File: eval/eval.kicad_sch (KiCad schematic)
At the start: 5 parts, among them J1 TC2030, U9 STM32G0B1CBTx

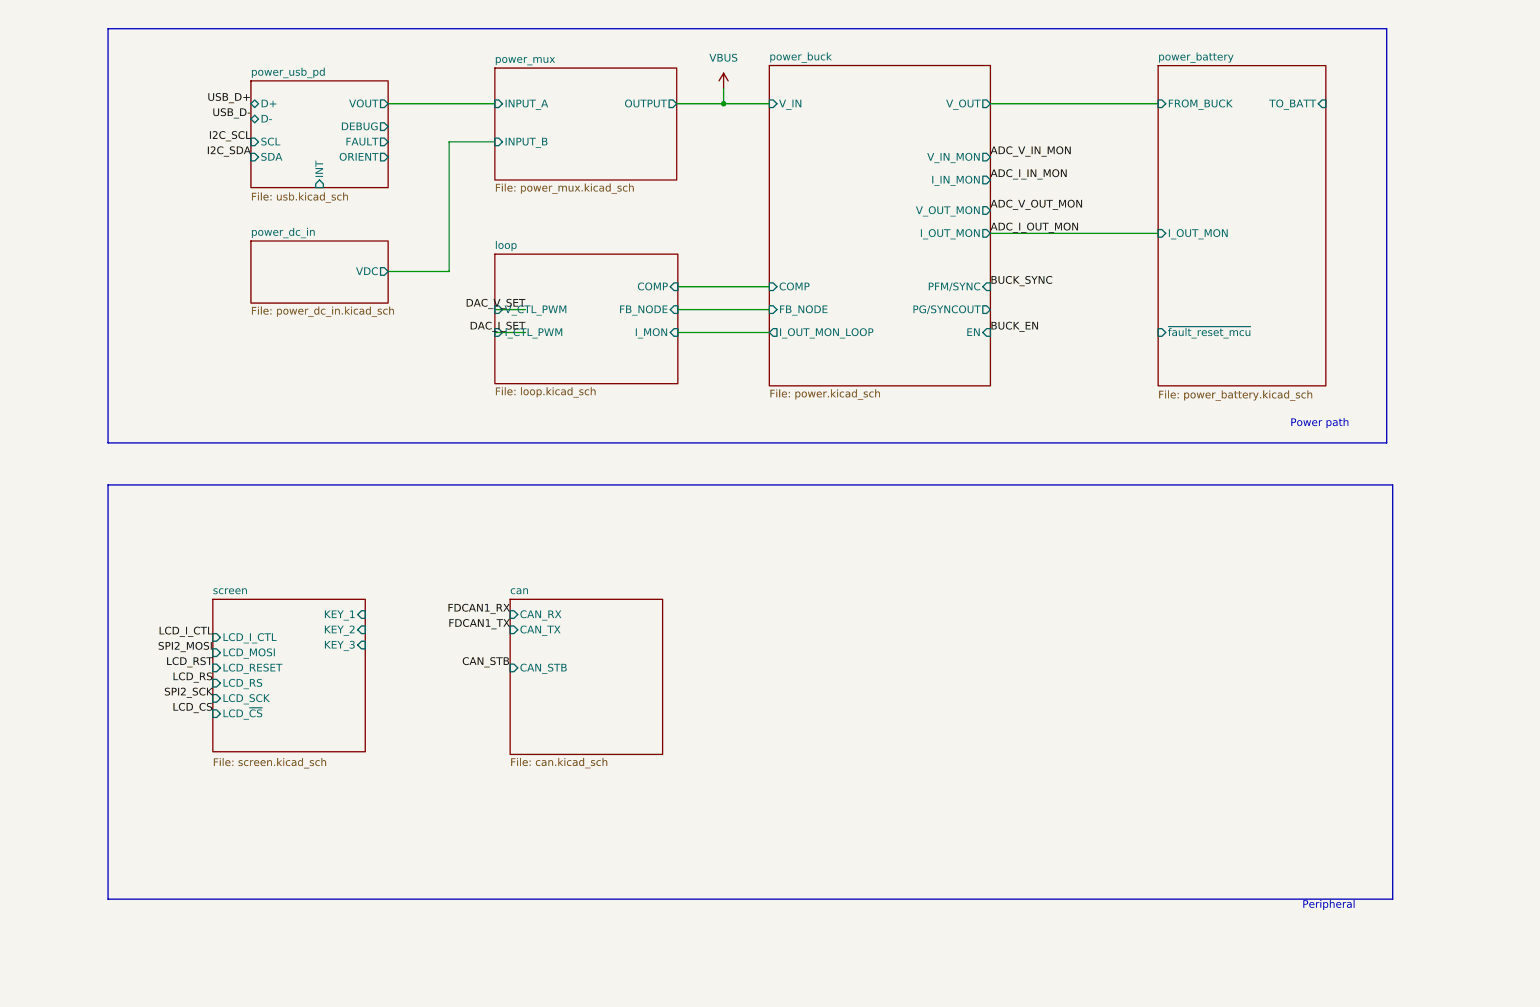
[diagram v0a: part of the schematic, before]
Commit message: [layout] group every function group together, ready for layout
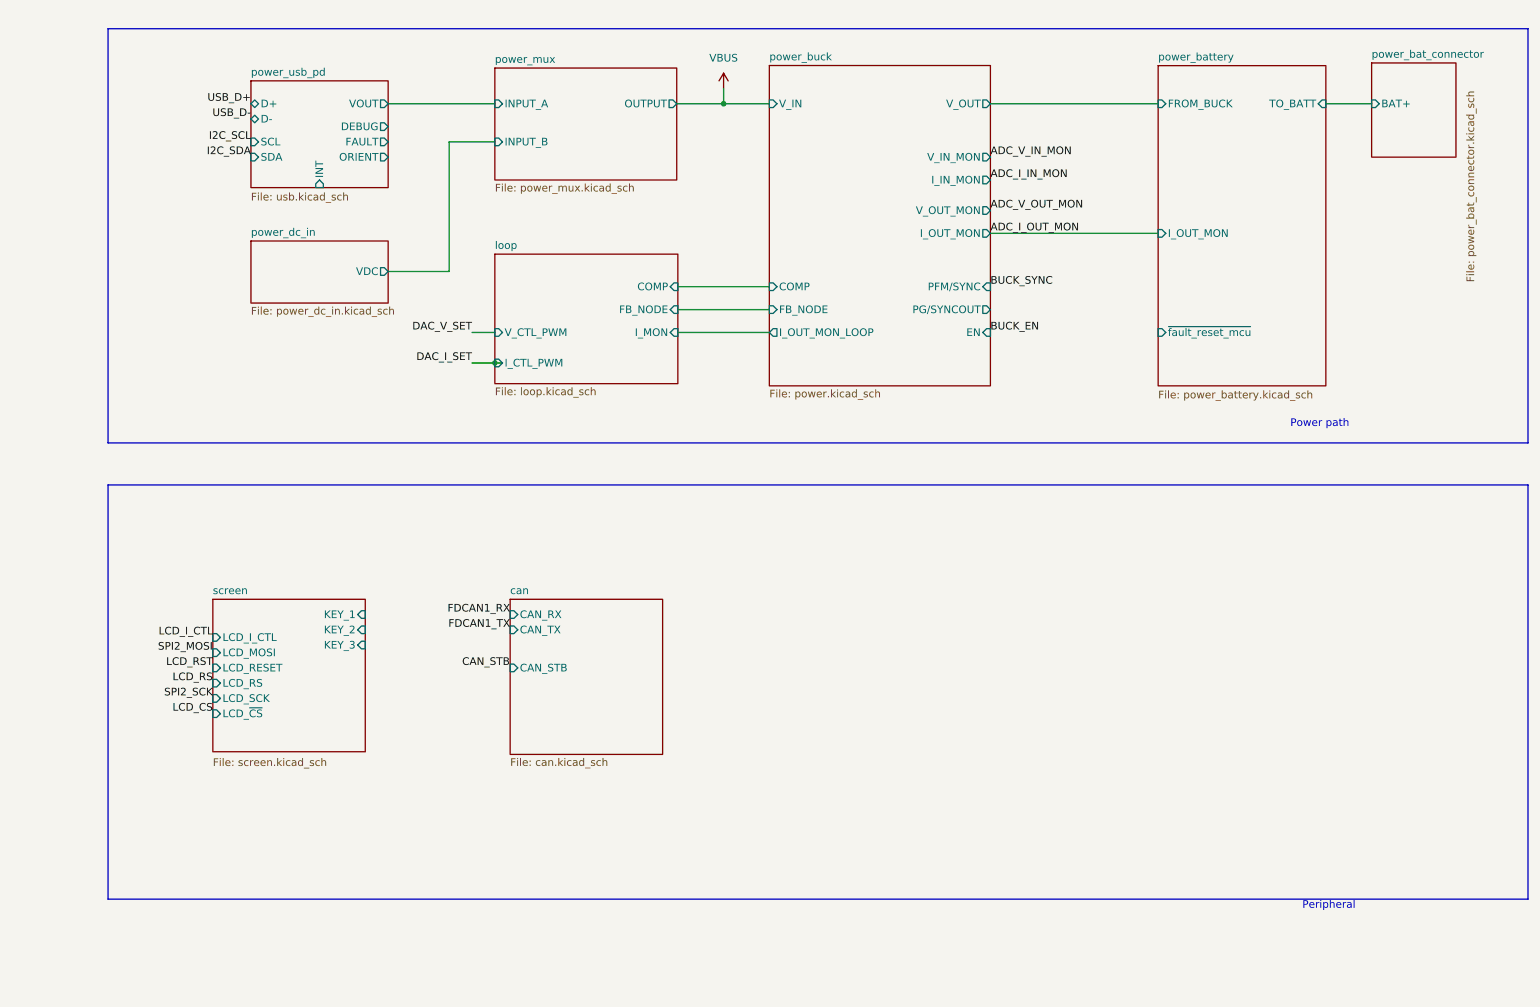
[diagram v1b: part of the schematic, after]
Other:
- added sheet power_bat_connector (power_bat_connector.kicad_sch)
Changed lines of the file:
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@@
 	(rectangle
 		(start 151.46 38.3)
-		(end 364.46 107.3)
+		(end 388 107.3)
 		(stroke
 			(width 0)
@@
 	(rectangle
 		(start 151.46 114.3)
-		(end 365.46 183.3)
+		(end 388 183.3)
 		(stroke
 			(width 0)
@@
 	)
 	(junction
+		(at 215.9 93.98)
+		(diameter 0)
+		(color 0 0 0 0)
+	)
+	(junction
 		(at 88.9 43.18)
 		(diameter 0)
@@
 	(wire
 		(pts
+			(xy 212.09 93.98) (xy 215.9 93.98)
+		)
+		(stroke
+			(width 0)
+			(type default)
+		)
+	)
+	(wire
+		(pts
 			(xy 198.12 78.74) (xy 208.28 78.74)
 		)
@@
 	(wire
 		(pts
-			(xy 215.9 88.9) (xy 220.98 88.9)
-		)
-		(stroke
-			(width 0)
-			(type default)
-		)
-	)
-	(wire
-		(pts
 			(xy 198.12 50.8) (xy 215.9 50.8)
 		)
@@
 	(wire
 		(pts
+			(xy 354.33 50.8) (xy 361.95 50.8)
+		)
+		(stroke
+			(width 0)
+			(type default)
+		)
+	)
+	(wire
+		(pts
 			(xy 80.01 157.48) (xy 80.01 154.94)
 		)
@@
 	(wire
 		(pts
+			(xy 215.9 93.98) (xy 217.17 93.98)
+		)
+		(stroke
+			(width 0)
+			(type default)
+		)
+	)
+	(wire
+		(pts
 			(xy 254 48.26) (xy 254 50.8)
 		)
@@
 	(wire
 		(pts
-			(xy 215.9 85.09) (xy 220.98 85.09)
+			(xy 215.9 88.9) (xy 212.09 88.9)
 		)
 		(stroke
@@
 	)
 	(label "DAC_I_SET"
-		(at 220.98 88.9 180)
+		(at 212.09 93.98 180)
 		(effects
 			(font
@@
 	)
 	(label "DAC_V_SET"
-		(at 220.98 85.09 180)
+		(at 212.09 88.9 180)
 		(effects
 			(font
@@
 	)
 	(sheet
+		(at 361.95 44)
+		(size 14.05 15.69)
+		(exclude_from_sim no)
+		(in_bom yes)
+		(on_board yes)
+		(dnp no)
+		(stroke
+			(width 0.1524)
+			(type solid)
+		)
+		(fill
+			(color 0 0 0 0)
+		)
+		(property "Sheetname" "power_bat_connector"
+			(at 361.95 43.2884 0)
+			(show_name no)
+			(do_not_autoplace no)
+			(effects
+				(font
+					(size 1.27 1.27)
+				)
+				(justify left bottom)
+			)
+		)
+		(property "Sheetfile" "power_bat_connector.kicad_sch"
+			(at 377.698 80.518 90)
+			(show_name no)
+			(do_not_autoplace no)
+			(effects
+				(font
+					(size 1.27 1.27)
+				)
+				(justify left top)
+			)
+		)
+		(pin "BAT+" input
+			(at 361.95 50.8 180)
+			(effects
+				(font
+					(size 1.27 1.27)
+				)
+				(justify left)
+			)
+		)
+		(instances
+			(project "eval"
+				(path "/8b023652-20db-48ce-ad53-bc2d9a4e5dd4"
+					(page "15")
+				)
+			)
+		)
+	)
+	(sheet
 		(at 215.9 75.85)
 		(size 30.48 21.58)
@@
 		)
 		(pin "I_CTL_PWM" input
-			(at 215.9 88.9 180)
+			(at 215.9 93.98 180)
 			(effects
 				(font
@@
 		)
 		(pin "V_CTL_PWM" input
-			(at 215.9 85.09 180)
-			(effects
-				(font
+			(at 215.9 88.9 180)
+			(effects
+				(font

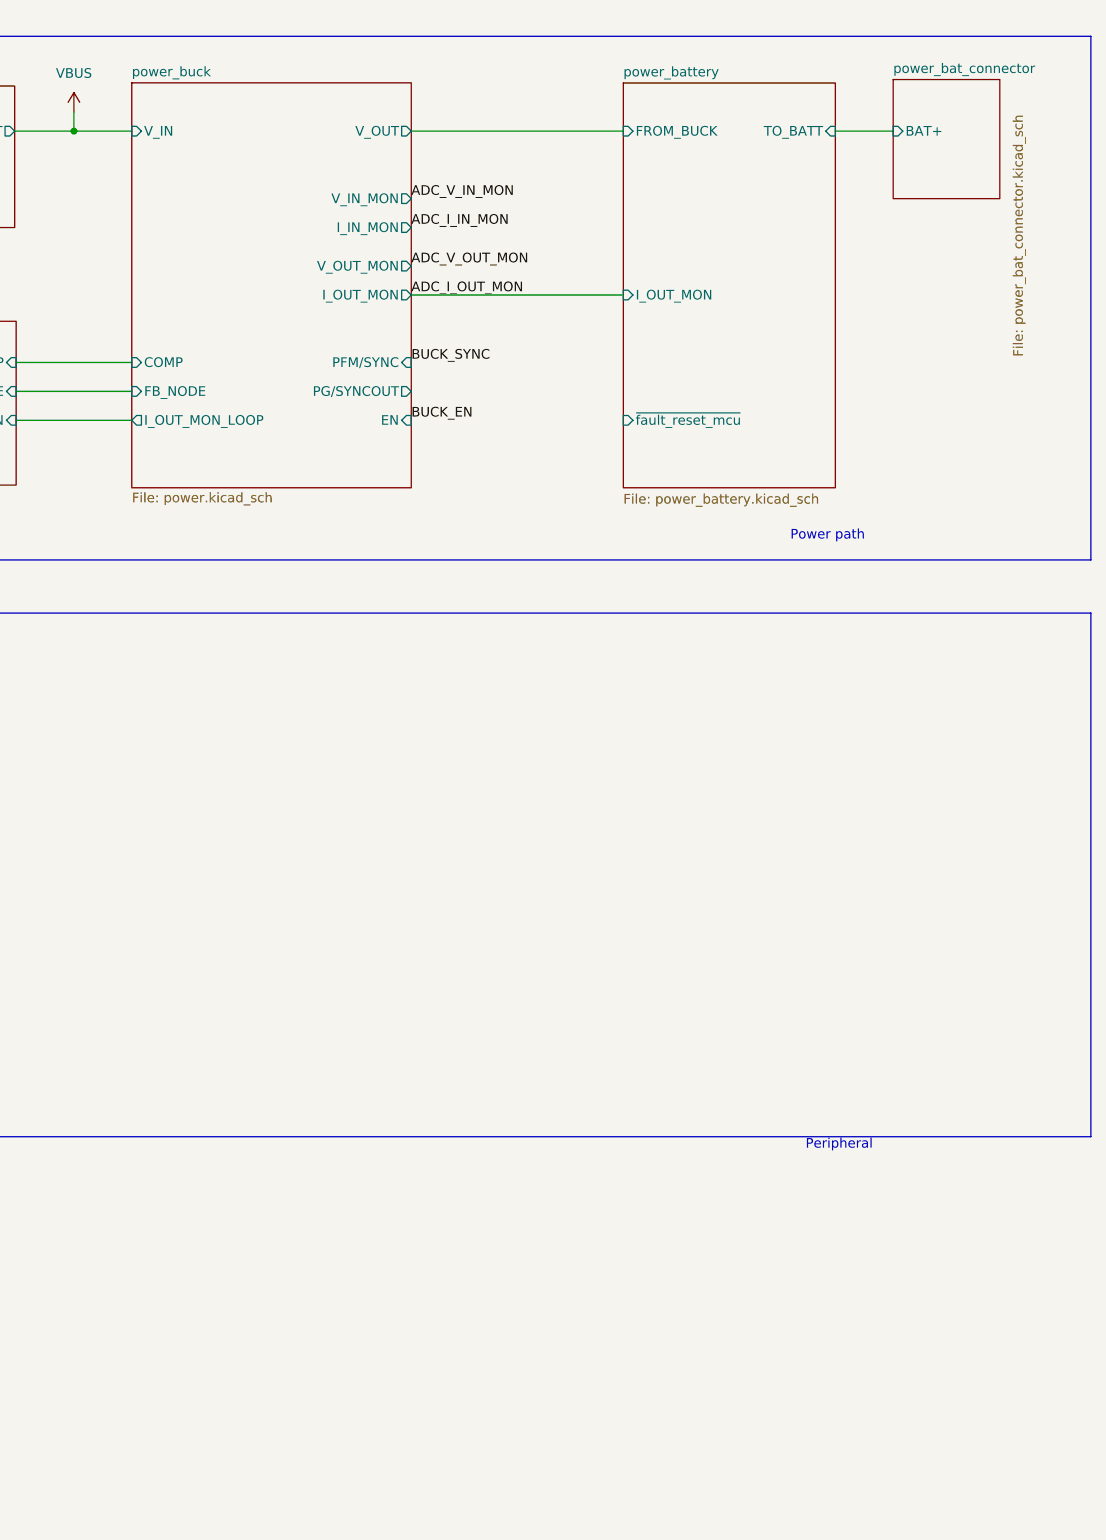
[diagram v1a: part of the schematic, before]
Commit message: [layout] fan on bottom side, power area on top
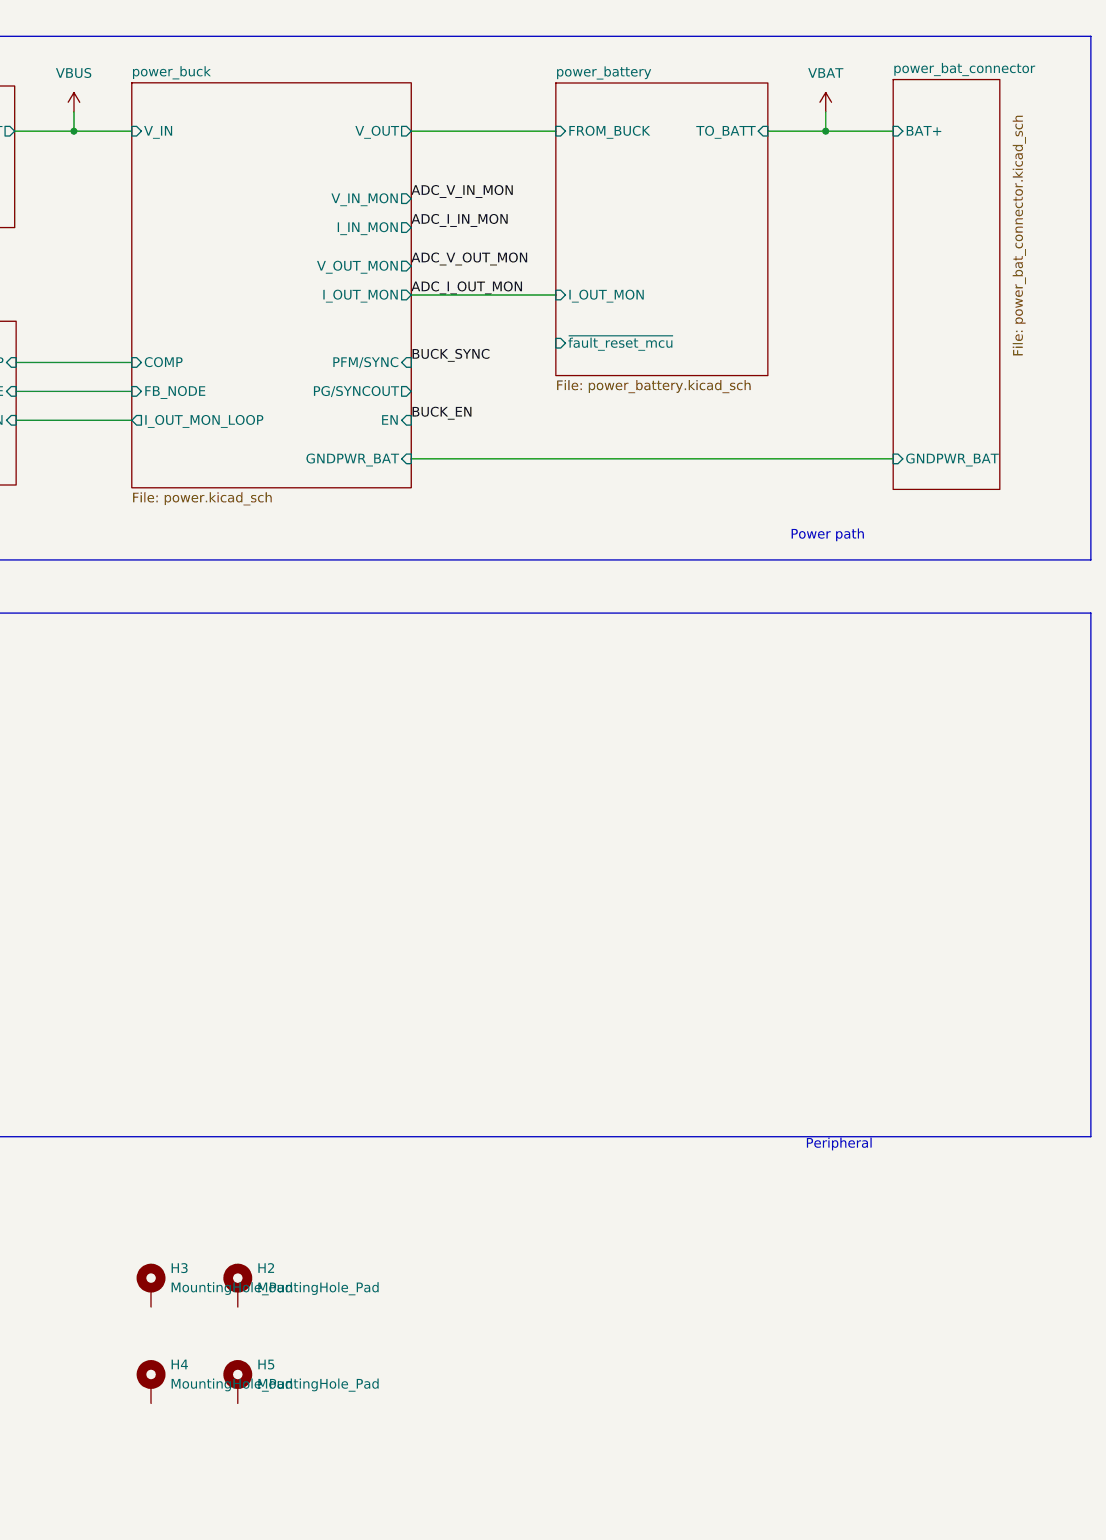
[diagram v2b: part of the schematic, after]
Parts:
- added H2, H3, H4, H5: MountingHole_Pad, MountingHole:MountingHole_2.2mm_M2_Pad_Via, symbol Mechanical:MountingHole_Pad
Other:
- sheet power_bat_connector ports: added GNDPWR_BAT; removed none
- sheet power_buck ports: added GNDPWR_BAT; removed none

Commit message: [layout] layout completed, ready for trace
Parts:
- added BZ1: Buzzer, symbol Device:Buzzer
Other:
- added sheet ntc (ntc.kicad_sch)
- added sheet ntc1 (ntc.kicad_sch)
- added sheet ntc2 (ntc.kicad_sch)

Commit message: [trace] add high power trace
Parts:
- renumbered C19 to C1, C20 to C2, C21 to C3, H3 to H1, H4 to H2, H2 to H3, H5 to H4, U9 to U1
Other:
- sheet loop ports: added I_CTL, V_CTL; removed I_CTL_PWM, V_CTL_PWM

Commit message: [trace] Add USB trace (with impedance control)
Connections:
- net ADC_I_IN_MON: now also U1.12 (PA1); no longer U1.13 (PA2)
- net ADC_I_OUT_MON: now also U1.19 (PB0); no longer U1.11 (PA0)
- net ADC_V_IN_MON: now also U1.11 (PA0); no longer U1.14 (PA3)
- net ADC_V_OUT_MON: no longer U1.12 (PA1)
- net ADC_V_OUT+_MON: now reaches U1.20 (PB1)
- net ADC_V_OUT-_MON: now reaches U1.21 (PB2)
- new net ADC_NTC_0: U1.13 (PA2)
- new net ADC_NTC_1: U1.14 (PA3)
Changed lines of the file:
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@@
-	(wire
-		(pts
-			(xy 107.95 83.82) (xy 107.95 82.55)
-		)
-		(stroke
-			(width 0)
-			(type default)
-		)
-	)
 	(wire
 		(pts
@@
 	)
 	(label "ADC_I_IN_MON"
+		(at 107.95 62.23 0)
+		(effects
+			(font
+				(size 1.27 1.27)
+			)
+			(justify left bottom)
+		)
+	)
+	(label "ADC_NTC_2"
+		(at 133.35 77.47 0)
+		(effects
+			(font
+				(size 1.27 1.27)
+			)
+			(justify left bottom)
+		)
+	)
+	(label "ADC_I_IN_MON"
 		(at 298.45 63.5 0)
 		(effects
@@
 		)
 	)
-	(label "ADC_I_OUT_MON"
+	(label "ADC_V_IN_MON"
 		(at 107.95 59.69 0)
 		(effects
@@
 		)
 	)
-	(label "ADC_I_IN_MON"
-		(at 107.95 64.77 0)
-		(effects
-			(font
-				(size 1.27 1.27)
-			)
-			(justify left bottom)
-		)
-	)
 	(label "ADC_V_OUT_MON"
 		(at 298.45 68.58 0)
@@
 		)
 	)
+	(label "ADC_I_OUT_MON"
+		(at 107.95 102.87 0)
+		(effects
+			(font
+				(size 1.27 1.27)
+			)
+			(justify left bottom)
+		)
+	)
 	(label "SYS_SWDCLK"
 		(at 63.5 195.58 0)
@@
 		)
 	)
-	(label "ADC_V_OUT_MON"
-		(at 107.95 62.23 0)
+	(label "ADC_V_OUT-_MON"
+		(at 107.95 107.95 0)
+		(effects
+			(font
+				(size 1.27 1.27)
+			)
+			(justify left bottom)
+		)
+	)
+	(label "ADC_NTC_1"
+		(at 107.95 67.31 0)
 		(effects
 			(font
@@
 	)
 	(label "USB_D-"
-		(at 107.95 83.82 0)
+		(at 107.95 82.55 0)
 		(effects
 			(font
@@
 		)
 	)
-	(label "ADC_V_IN_MON"
-		(at 107.95 67.31 0)
-		(effects
-			(font
-				(size 1.27 1.27)
-			)
-			(justify left bottom)
-		)
-	)
 	(label "FDCAN1_RX"
 		(at 107.95 123.19 0)
@@
 		)
 	)
+	(label "ADC_NTC_0"
+		(at 107.95 64.77 0)
+		(effects
+			(font
+				(size 1.27 1.27)
+			)
+			(justify left bottom)
+		)
+	)
 	(label "SPI2_MOSI"
 		(at 168.91 142.24 180)
@@
 		)
 	)
+	(label "ADC_V_OUT+_MON"
+		(at 107.95 105.41 0)
+		(effects
+			(font
+				(size 1.27 1.27)
+			)
+			(justify left bottom)
+		)
+	)
